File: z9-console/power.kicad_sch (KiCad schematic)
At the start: 29 parts, among them U5 TLV76733DRVx, U6 B0505XT-1WR3, U7 LMR14006YDDCR

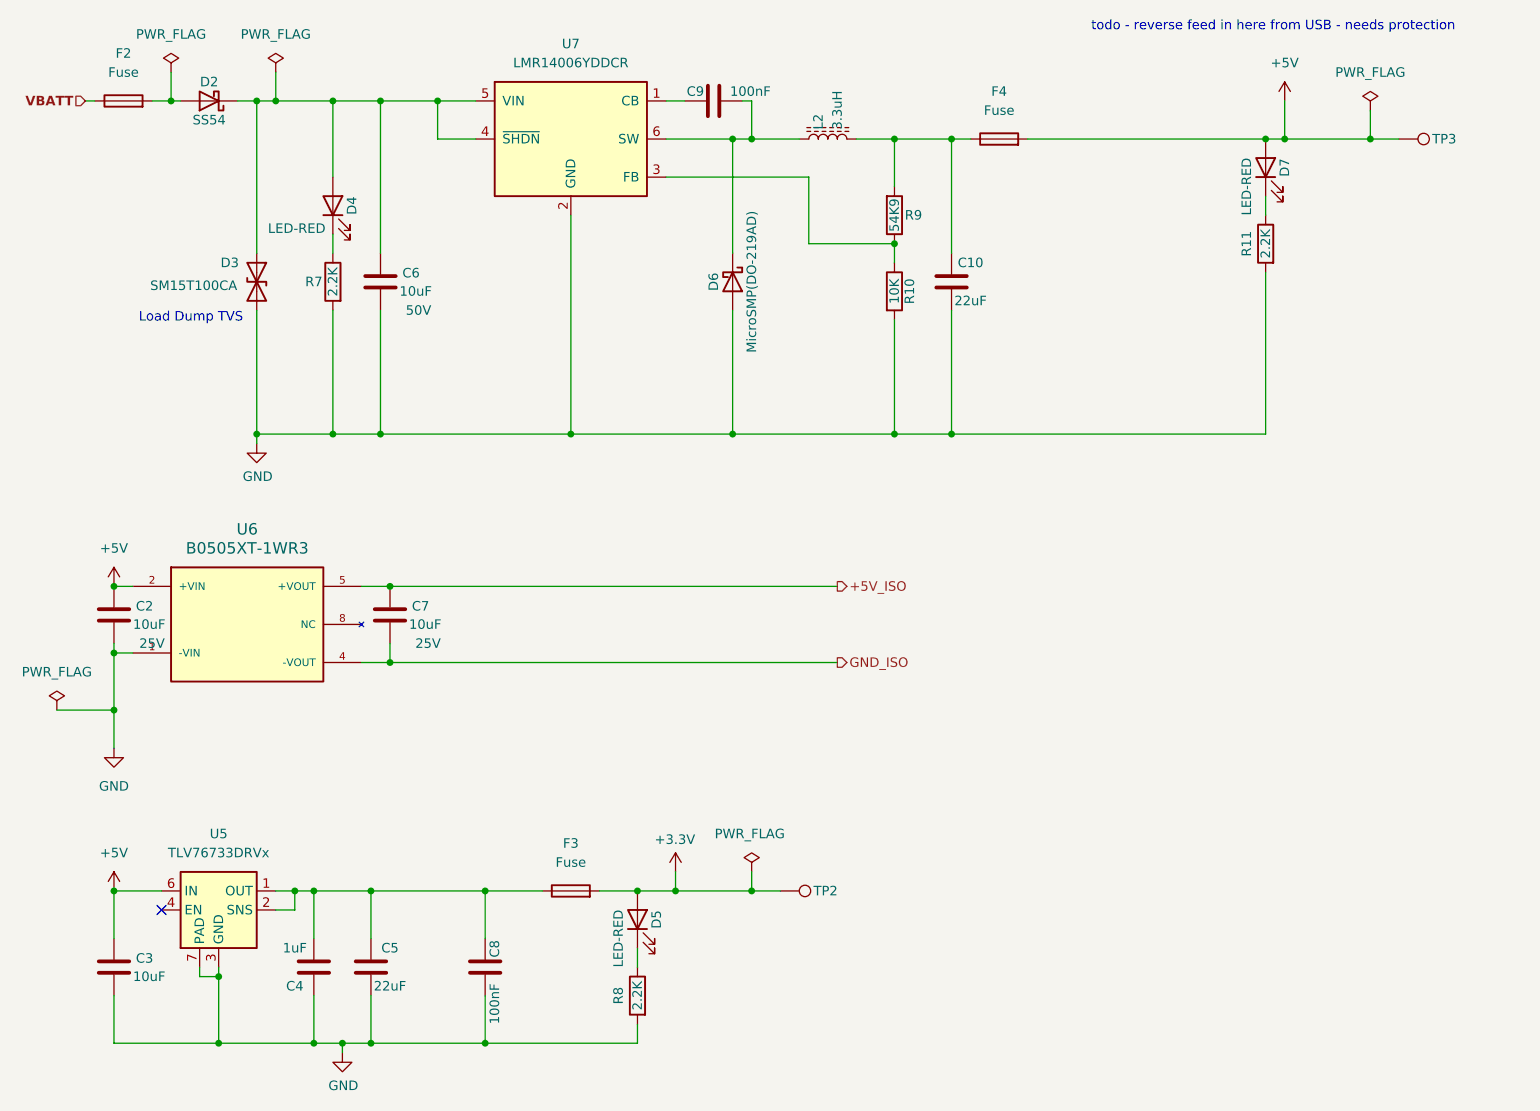
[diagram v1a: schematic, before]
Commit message: fix 10uf 25v
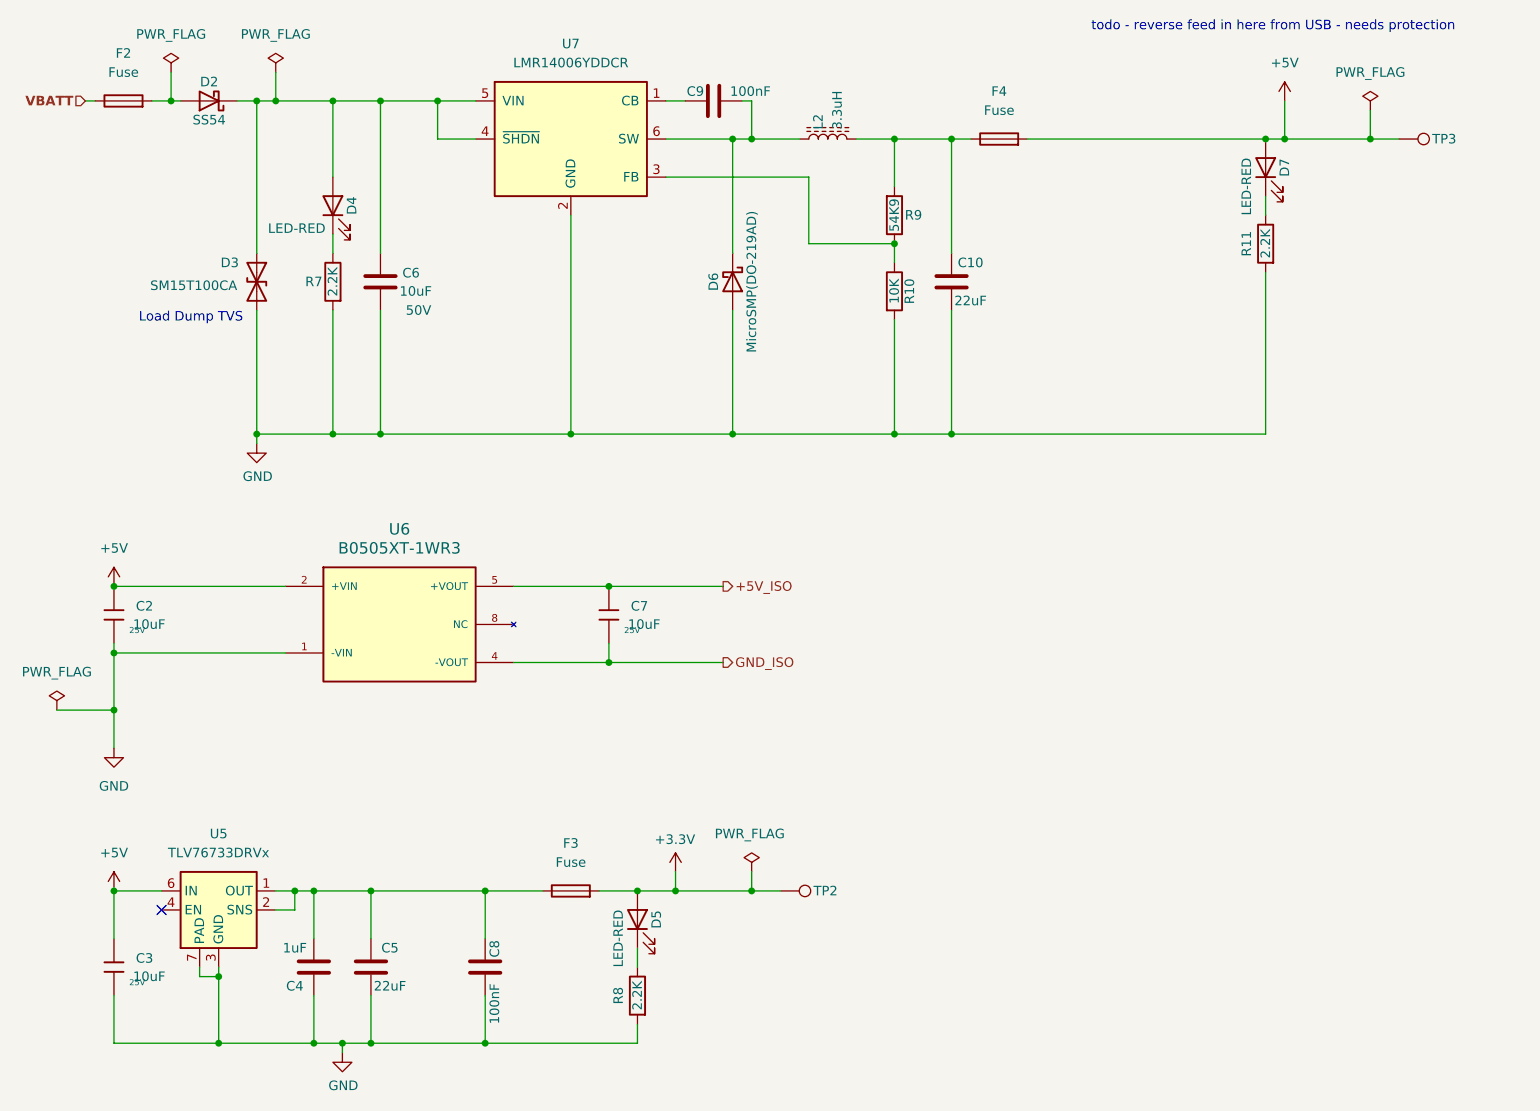
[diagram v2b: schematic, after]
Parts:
- C2, C7: footprint Capacitor_SMD:C_0603_1608Metric -> dnt:C_0603_1608Metric; symbol Device:C -> dnt_global:0603,10uF,_25V; Attrition Qty (none) -> 8; Capacitance (none) -> 10uF; Category (none) -> Capacitors,Multilayer Ceramic Capacitors MLCC - SMD/SMT; Class (none) -> Basic Component; Manufacturer (none) -> Samsung Electro-Mechanics; Minimum Qty (none) -> 20; Part (none) -> CL10A106MA8NRNC; Price (none) -> 0.021USD; Process (none) -> SMT; Stock (none) -> 3388297; Temperature Coefficient (none) -> X5R; Tolerance (none) -> ±20%; Voltage 25V -> (none); Voltage Rated (none) -> 25V
- C3: footprint Capacitor_SMD:C_0603_1608Metric -> dnt:C_0603_1608Metric; symbol Device:C -> dnt_global:0603,10uF,_25V; Attrition Qty (none) -> 8; Capacitance (none) -> 10uF; Category (none) -> Capacitors,Multilayer Ceramic Capacitors MLCC - SMD/SMT; Class (none) -> Basic Component; Manufacturer (none) -> Samsung Electro-Mechanics; Minimum Qty (none) -> 20; Part (none) -> CL10A106MA8NRNC; Price (none) -> 0.021USD; Process (none) -> SMT; Stock (none) -> 3388297; Temperature Coefficient (none) -> X5R; Tolerance (none) -> ±20%; Voltage Rated (none) -> 25V
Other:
- moved on the sheet: C7, U6

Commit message: continue lssc fixups
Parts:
- C8, C9: footprint Capacitor_SMD:C_0603_1608Metric -> dnt:C_0603_1608Metric; symbol Device:C -> dnt_global:0603,100nF; Attrition Qty (none) -> 10; Capacitance (none) -> 100nF; Category (none) -> Capacitors,Multilayer Ceramic Capacitors MLCC - SMD/SMT; Class (none) -> Basic Component; Minimum Qty (none) -> 20; Part (none) -> CC0603KRX7R9BB104; Part Number CC0603KRX7R9BB104 -> (none); Price (none) -> 0.006USD; Process (none) -> SMT; Stock (none) -> 70324515; Temperature Coefficient (none) -> X7R; Tolerance (none) -> ±10%; Voltage Rated (none) -> 50V
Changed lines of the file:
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@@
 	)
 	(symbol
-		(lib_id "Device:C")
+		(lib_id "dnt_global:0603,100nF")
 		(at 78.74 149.86 0)
 		(unit 1)
@@
 			)
 		)
-		(property "Footprint" "Capacitor_SMD:C_0603_1608Metric"
-			(at -41.148 109.22 90)
-			(effects
-				(font
-					(size 1.524 1.524)
-				)
-				(hide yes)
-			)
-		)
-		(property "Datasheet" "~"
+		(property "Footprint" "dnt:C_0603_1608Metric"
+			(at 76.962 149.86 90)
+			(effects
+				(font
+					(size 1.27 1.27)
+				)
+				(hide yes)
+			)
+		)
+		(property "Datasheet" "https://www.lcsc.com/datasheet/lcsc_datasheet_2211101700_YAGEO-CC0603KRX7R9BB104_C14663.pdf"
 			(at 78.74 149.86 0)
 			(effects
 				(font
-					(size 1.524 1.524)
-				)
-				(hide yes)
-			)
-		)
-		(property "Description" "Unpolarized capacitor"
+					(size 1.27 1.27)
+				)
+				(hide yes)
+			)
+		)
+		(property "Description" "50V 100nF X7R ±10% 0603 Multilayer Ceramic Capacitors MLCC - SMD/SMT ROHS"
 			(at 78.74 149.86 0)
 			(effects
@@
 			)
 		)
-		(property "Sim.Device" ""
+		(property "Stock" "70324515"
 			(at 78.74 149.86 0)
 			(effects
@@
 			)
 		)
-		(property "Sim.Pins" ""
+		(property "Price" "0.006USD"
 			(at 78.74 149.86 0)
 			(effects
@@
 			)
 		)
-		(property "Voltage" ""
-			(at 78.74 149.86 90)
-			(effects
-				(font
-					(size 1.27 1.27)
-				)
-				(hide yes)
-			)
-		)
-		(property "Silkscreen" ""
+		(property "Process" "SMT"
 			(at 78.74 149.86 0)
 			(effects
@@
 			)
 		)
-		(property "Part Number" "CC0603KRX7R9BB104 "
-			(at 78.74 149.86 90)
+		(property "Minimum Qty" "20"
+			(at 78.74 149.86 0)
+			(effects
+				(font
+					(size 1.27 1.27)
+				)
+				(hide yes)
+			)
+		)
+		(property "Attrition Qty" "10"
+			(at 78.74 149.86 0)
+			(effects
+				(font
+					(size 1.27 1.27)
+				)
+				(hide yes)
+			)
+		)
+		(property "Class" "Basic Component"
+			(at 78.74 149.86 0)
+			(effects
+				(font
+					(size 1.27 1.27)
+				)
+				(hide yes)
+			)
+		)
+		(property "Category" "Capacitors,Multilayer Ceramic Capacitors MLCC - SMD/SMT"
+			(at 78.74 149.86 0)
+			(effects
+				(font
+					(size 1.27 1.27)
+				)
+				(hide yes)
+			)
+		)
+		(property "Part" "CC0603KRX7R9BB104"
+			(at 78.74 149.86 0)
+			(effects
+				(font
+					(size 1.27 1.27)
+				)
+				(hide yes)
+			)
+		)
+		(property "Voltage Rated" "50V"
+			(at 80.772 151.9062 0)
+			(effects
+				(font
+					(size 0.8 0.8)
+				)
+				(justify left)
+			)
+		)
+		(property "Tolerance" "±10%"
+			(at 78.74 149.86 0)
+			(effects
+				(font
+					(size 1.27 1.27)
+				)
+				(hide yes)
+			)
+		)
+		(property "Capacitance" "100nF"
+			(at 78.74 149.86 0)
+			(effects
+				(font
+					(size 1.27 1.27)
+				)
+				(hide yes)
+			)
+		)
+		(property "Temperature Coefficient" "X7R"
+			(at 78.74 149.86 0)
 			(effects
 				(font
@@
 	)
 	(symbol
-		(lib_id "Device:C")
+		(lib_id "dnt_global:0603,100nF")
 		(at 109.22 34.29 90)
 		(unit 1)
@@
 			)
 		)
-		(property "Footprint" "Capacitor_SMD:C_0603_1608Metric"
-			(at 68.58 154.178 90)
-			(effects
-				(font
-					(size 1.524 1.524)
-				)
-				(hide yes)
-			)
-		)
-		(property "Datasheet" "~"
+		(property "Footprint" "dnt:C_0603_1608Metric"
+			(at 109.22 36.068 90)
+			(effects
+				(font
+					(size 1.27 1.27)
+				)
+				(hide yes)
+			)
+		)
+		(property "Datasheet" "https://www.lcsc.com/datasheet/lcsc_datasheet_2211101700_YAGEO-CC0603KRX7R9BB104_C14663.pdf"
 			(at 109.22 34.29 0)
 			(effects
 				(font
-					(size 1.524 1.524)
-				)
-				(hide yes)
-			)
-		)
-		(property "Description" "Unpolarized capacitor"
+					(size 1.27 1.27)
+				)
+				(hide yes)
+			)
+		)
+		(property "Description" "50V 100nF X7R ±10% 0603 Multilayer Ceramic Capacitors MLCC - SMD/SMT ROHS"
 			(at 109.22 34.29 0)
 			(effects
@@
 			)
 		)
-		(property "Sim.Device" ""
+		(property "Stock" "70324515"
 			(at 109.22 34.29 0)
 			(effects
@@
 			)
 		)
-		(property "Sim.Pins" ""
+		(property "Price" "0.006USD"
 			(at 109.22 34.29 0)
 			(effects
@@
 			)
 		)
-		(property "Voltage" ""
-			(at 109.22 34.29 90)
-			(effects
-				(font
-					(size 1.27 1.27)
-				)
-				(hide yes)
-			)
-		)
-		(property "Silkscreen" ""
+		(property "Process" "SMT"
 			(at 109.22 34.29 0)
 			(effects
@@
 			)
 		)
-		(property "Part Number" "CC0603KRX7R9BB104 "
-			(at 109.22 34.29 90)
-			(effects
-				(font
+		(property "Minimum Qty" "20"
+			(at 109.22 34.29 0)
+			(effects
+				(font
+					(size 1.27 1.27)
+				)
+				(hide yes)
+			)
+		)
+		(property "Attrition Qty" "10"
+			(at 109.22 34.29 0)
+			(effects
+				(font
+					(size 1.27 1.27)
+				)
+				(hide yes)
+			)
+		)
+		(property "Class" "Basic Component"
+			(at 109.22 34.29 0)
+			(effects
+				(font
+					(size 1.27 1.27)
+				)
+				(hide yes)
+			)
+		)
+		(property "Category" "Capacitors,Multilayer Ceramic Capacitors MLCC - SMD/SMT"
+			(at 109.22 34.29 0)
+			(effects
+				(font
+					(size 1.27 1.27)
+				)
+				(hide yes)
+			)
+		)
+		(property "Part" "CC0603KRX7R9BB104"
+			(at 109.22 34.29 0)
+			(effects
+				(font
+					(size 1.27 1.27)
+				)
+				(hide yes)
+			)
+		)
+		(property "Voltage Rated" "50V"
+			(at 111.2662 32.258 0)
+			(effects
+				(font
+					(size 0.8 0.8)
+				)
+				(justify left)
+			)
+		)
+		(property "Tolerance" "±10%"
+			(at 109.22 34.29 0)
+			(effects
+				(font
+					(size 1.27 1.27)
+				)
+				(hide yes)
+			)
+		)
+		(property "Capacitance" "100nF"
+			(at 109.22 34.29 0)
+			(effects
+				(font
+					(size 1.27 1.27)
+				)
+				(hide yes)
+			)
+		)
+		(property "Temperature Coefficient" "X7R"
+			(at 109.22 34.29 0)
+			(effects
+				(font

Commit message: lcsc changes done - export for prod
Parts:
- R10: footprint PCM_JLCPCB:R_0402 -> dnt:R_0402_1005Metric; symbol dnt_global:Resistor_0402,10kΩ -> dnt_global:0402,10kΩ
- R11, R7, R8: symbol dnt_global:Resistor_0402,10kΩ -> PCM_JLCPCB-Resistors:0402,2.2kΩ; LCSC C25744 -> C25879; Part 0402WGF1002TCE -> 0402WGF2201TCE; Resistance 10kΩ -> 2.2kΩ; Stock 24372091 -> 1767502
- R9: symbol dnt_global:Resistor_0402,10kΩ -> PCM_JLCPCB-Resistors:0402,56kΩ; Class Basic Component -> Preferred Component; LCSC C25744 -> C25796; Part 0402WGF1002TCE -> 0402WGF5602TCE; Resistance 10kΩ -> 56kΩ; Stock 24372091 -> 478348
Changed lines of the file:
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@@
 	)
 	(symbol
-		(lib_id "dnt_global:Resistor_0402,10kΩ")
+		(lib_id "PCM_JLCPCB-Resistors:0402,2.2kΩ")
 		(at 58.42 58.42 180)
 		(unit 1)
@@
 			)
 		)
-		(property "Datasheet" "https://www.lcsc.com/datasheet/lcsc_datasheet_2411221126_UNI-ROYAL-Uniroyal-Elec-0402WGF1002TCE_C25744.pdf"
+		(property "Datasheet" "https://www.lcsc.com/datasheet/lcsc_datasheet_2206010045_UNI-ROYAL-Uniroyal-Elec-0402WGF2201TCE_C25879.pdf"
 			(at 58.42 58.42 0)
 			(effects
@@
 			)
 		)
-		(property "Description" "62.5mW Thick Film Resistors 50V ±100ppm/°C ±1% 10kΩ 0402 Chip Resistor - Surface Mount ROHS"
+		(property "Description" "62.5mW Thick Film Resistors 50V ±100ppm/°C ±1% 2.2kΩ 0402 Chip Resistor - Surface Mount ROHS"
 			(at 58.42 58.42 0)
 			(effects
@@
 			)
 		)
-		(property "LCSC" "C25744"
+		(property "LCSC" "C25879"
 			(at 58.42 58.42 0)
 			(effects
@@
 			)
 		)
-		(property "Stock" "24372091"
+		(property "Stock" "1767502"
 			(at 58.42 58.42 0)
 			(effects
@@
 			)
 		)
-		(property "Part" "0402WGF1002TCE"
+		(property "Part" "0402WGF2201TCE"
 			(at 58.42 58.42 0)
 			(effects
@@
 			)
 		)
-		(property "Resistance" "10kΩ"
+		(property "Resistance" "2.2kΩ"
 			(at 58.42 58.42 0)
 			(effects
@@
 	)
 	(symbol
-		(lib_id "dnt_global:Resistor_0402,10kΩ")
+		(lib_id "PCM_JLCPCB-Resistors:0402,56kΩ")
 		(at 133.35 49.53 0)
 		(unit 1)
@@
 			)
 		)
-		(property "Datasheet" "https://www.lcsc.com/datasheet/lcsc_datasheet_2411221126_UNI-ROYAL-Uniroyal-Elec-0402WGF1002TCE_C25744.pdf"
+		(property "Datasheet" "https://www.lcsc.com/datasheet/lcsc_datasheet_2411221126_UNI-ROYAL-Uniroyal-Elec-0402WGF5602TCE_C25796.pdf"
 			(at 133.35 49.53 0)
 			(effects
@@
 			)
 		)
-		(property "Description" "62.5mW Thick Film Resistors 50V ±100ppm/°C ±1% 10kΩ 0402 Chip Resistor - Surface Mount ROHS"
+		(property "Description" "62.5mW Thick Film Resistors 50V ±100ppm/°C ±1% 56kΩ 0402 Chip Resistor - Surface Mount ROHS"
 			(at 133.35 49.53 0)
 			(effects
@@
 			)
 		)
-		(property "LCSC" "C25744"
+		(property "LCSC" "C25796"
 			(at 133.35 49.53 0)
 			(effects
@@
 			)
 		)
-		(property "Stock" "24372091"
+		(property "Stock" "478348"
 			(at 133.35 49.53 0)
 			(effects
@@
 			)
 		)
-		(property "Class" "Basic Component"
+		(property "Class" "Preferred Component"
 			(at 133.35 49.53 0)
 			(effects
@@
 			)
 		)
-		(property "Part" "0402WGF1002TCE"
+		(property "Part" "0402WGF5602TCE"
 			(at 133.35 49.53 0)
 			(effects
@@
 			)
 		)
-		(property "Resistance" "10kΩ"
+		(property "Resistance" "56kΩ"
 			(at 133.35 49.53 0)
 			(effects
@@
 	)
 	(symbol
-		(lib_id "dnt_global:Resistor_0402,10kΩ")
+		(lib_id "PCM_JLCPCB-Resistors:0402,2.2kΩ")
 		(at 182.88 53.34 180)
 		(unit 1)
@@
 			)
 		)
-		(property "Datasheet" "https://www.lcsc.com/datasheet/lcsc_datasheet_2411221126_UNI-ROYAL-Uniroyal-Elec-0402WGF1002TCE_C25744.pdf"
+		(property "Datasheet" "https://www.lcsc.com/datasheet/lcsc_datasheet_2206010045_UNI-ROYAL-Uniroyal-Elec-0402WGF2201TCE_C25879.pdf"
 			(at 182.88 53.34 0)
 			(effects
@@
 			)
 		)
-		(property "Description" "62.5mW Thick Film Resistors 50V ±100ppm/°C ±1% 10kΩ 0402 Chip Resistor - Surface Mount ROHS"
+		(property "Description" "62.5mW Thick Film Resistors 50V ±100ppm/°C ±1% 2.2kΩ 0402 Chip Resistor - Surface Mount ROHS"
 			(at 182.88 53.34 0)
 			(effects
@@
 			)
 		)
-		(property "LCSC" "C25744"
+		(property "LCSC" "C25879"
 			(at 182.88 53.34 0)
 			(effects
@@
 			)
 		)
-		(property "Stock" "24372091"
+		(property "Stock" "1767502"
 			(at 182.88 53.34 0)
 			(effects
@@
 			)
 		)
-		(property "Part" "0402WGF1002TCE"
+		(property "Part" "0402WGF2201TCE"
 			(at 182.88 53.34 0)
 			(effects
@@
 			)
 		)
-		(property "Resistance" "10kΩ"
+		(property "Resistance" "2.2kΩ"
 			(at 182.88 53.34 0)
 			(effects
@@
 	)
 	(symbol
-		(lib_id "dnt_global:Resistor_0402,10kΩ")
+		(lib_id "dnt_global:0402,10kΩ")
 		(at 133.35 59.69 0)
 		(mirror x)
@@
 			)
 		)
-		(property "Footprint" "PCM_JLCPCB:R_0402"
+		(property "Footprint" "dnt:R_0402_1005Metric"
 			(at 131.572 59.69 90)
 			(effects
@@
 	)
 	(symbol
-		(lib_id "dnt_global:Resistor_0402,10kΩ")
+		(lib_id "PCM_JLCPCB-Resistors:0402,2.2kΩ")
 		(at 99.06 153.67 180)
 		(unit 1)
@@
 			)
 		)
-		(property "Datasheet" "https://www.lcsc.com/datasheet/lcsc_datasheet_2411221126_UNI-ROYAL-Uniroyal-Elec-0402WGF1002TCE_C25744.pdf"
+		(property "Datasheet" "https://www.lcsc.com/datasheet/lcsc_datasheet_2206010045_UNI-ROYAL-Uniroyal-Elec-0402WGF2201TCE_C25879.pdf"
 			(at 99.06 153.67 0)
 			(effects
@@
 			)
 		)
-		(property "Description" "62.5mW Thick Film Resistors 50V ±100ppm/°C ±1% 10kΩ 0402 Chip Resistor - Surface Mount ROHS"
+		(property "Description" "62.5mW Thick Film Resistors 50V ±100ppm/°C ±1% 2.2kΩ 0402 Chip Resistor - Surface Mount ROHS"
 			(at 99.06 153.67 0)
 			(effects
@@
 			)
 		)
-		(property "LCSC" "C25744"
+		(property "LCSC" "C25879"
 			(at 99.06 153.67 0)
 			(effects
@@
 			)
 		)
-		(property "Stock" "24372091"
+		(property "Stock" "1767502"
 			(at 99.06 153.67 0)
 			(effects
@@
 			)
 		)
-		(property "Part" "0402WGF1002TCE"
+		(property "Part" "0402WGF2201TCE"
 			(at 99.06 153.67 0)
 			(effects
@@
 			)
 		)
-		(property "Resistance" "10kΩ"
+		(property "Resistance" "2.2kΩ"
 			(at 99.06 153.67 0)
 			(effects

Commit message: more change - generarte jlc
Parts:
- U6: JLCPCB Rotation Offset 270 -> 0
- U7: JLCPCB Rotation Offset -90 -> 0
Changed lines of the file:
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@@
 			)
 		)
-		(property "JLCPCB Rotation Offset" "270"
+		(property "JLCPCB Rotation Offset" "0"
 			(at 67.31 125.984 0)
 			(effects
@@
 			)
 		)
-		(property "JLCPCB Rotation Offset" "-90"
+		(property "JLCPCB Rotation Offset" "0"
 			(at 90.17 39.37 0)
 			(effects

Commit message: more moving offset to library - tedious
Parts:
- U6: FT Rotation Offset (none) -> 270; JLCPCB Rotation Offset 0 -> (none)
- U7: symbol Regulator_Switching:LMR14206 -> dnt_global:LMR14006YDDCR; FT Rotation Offset (none) -> 90; JLCPCB Rotation Offset 0 -> (none); Order https://jlcpcb.com/partdetail/TexasInstruments-LMR14006YDDC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 -> (none); Package TSOT-23-6 -> (none)
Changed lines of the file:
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@@
 			)
 		)
-		(property "Datasheet" "B0505S-1WR2"
+		(property "Datasheet" ""
 			(at 67.818 121.412 0)
 			(effects
@@
 			)
 		)
-		(property "JLCPCB Rotation Offset" "0"
+		(property "FT Rotation Offset" "270"
 			(at 67.31 125.984 0)
 			(effects
@@
 	)
 	(symbol
-		(lib_id "Regulator_Switching:LMR14206")
+		(lib_id "dnt_global:LMR14006YDDCR")
 		(at 90.17 39.37 0)
 		(unit 1)
@@
 			)
 		)
-		(property "Datasheet" "http://www.ti.com/lit/ds/symlink/lmr14206.pdf"
+		(property "Datasheet" "https://www.ti.com/cn/lit/gpn/lmr14006"
 			(at 80.01 27.94 0)
 			(effects
@@
 			)
 		)
-		(property "Description" "Simple Switcher Buck Regulator, Vin=4.5-42V, Iout=600mA, Adjustable output voltage, SOT-23-6 package"
+		(property "Description" "-40℃~+125℃@(TJ) 1 2.1MHz 28uA 4V~40V 600mA 765mV~38.4V Adjustable Buck Buck Built-In No TSOT-23-6 DC-DC Converters ROHS"
 			(at 90.17 39.37 0)
 			(effects
@@
 			)
 		)
-		(property "Package" " TSOT-23-6"
+		(property "FT Rotation Offset" "90"
 			(at 90.17 39.37 0)
 			(effects
-				(font
-					(size 1.27 1.27)
-				)
-				(hide yes)
-			)
-		)
-		(property "Order" "https://jlcpcb.com/partdetail/TexasInstruments-LMR14006YDDCR/C477919"
-			(at 90.17 39.37 0)
-			(effects
-				(font
-					(size 1.27 1.27)
-				)
-				(hide yes)
-			)
-		)
-		(property "JLCPCB Rotation Offset" "0"
-			(at 90.17 39.37 0)
-			(effects

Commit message: ism issues
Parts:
- D6: value MicroSMP(DO-219AD) -> V1P6-M3/H 60V 1A
- R9: value 54K9 -> 56K
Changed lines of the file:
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@@
 			)
 		)
-		(property "Value" "MicroSMP(DO-219AD)"
-			(at 114.3 58.42 0)
+		(property "Value" "V1P6-M3/H 60V 1A"
+			(at 112.522 81.788 90)
 			(effects
 				(font
@@
 	)
 	(symbol
+		(lib_name "Fuse_16V_500mA_100A_1A_150mΩ_0805_PTC_Resettable_Fuses_ROHS_1")
 		(lib_id "dnt_global:Fuse_16V_500mA_100A_1A_150mΩ_0805_PTC_Resettable_Fuses_ROHS")
 		(at 147.32 39.37 90)
@@
 			)
 		)
-		(property "Value" "54K9"
+		(property "Value" "56K"
 			(at 133.35 49.53 90)
 			(effects
